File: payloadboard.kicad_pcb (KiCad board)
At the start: 2 copper layers, 46.8 x 46.8 mm, 15 parts, among them J1 TFM-110-12-L-D-A, J2 FLE-105-01-G-DV-A, J3 Micro_SD_Card, Q4 MMBT2907

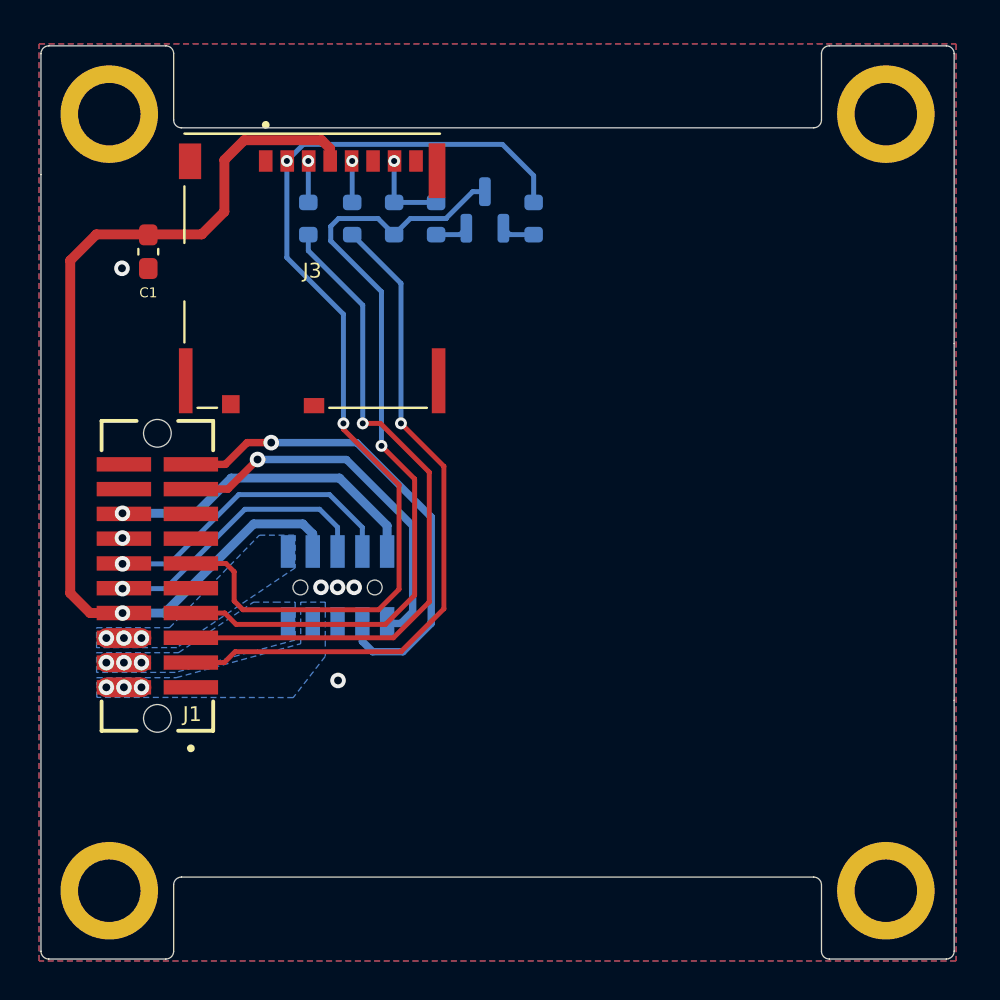
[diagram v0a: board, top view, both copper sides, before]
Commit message: Added 3.3V power regulator with enable pin and new stack connector
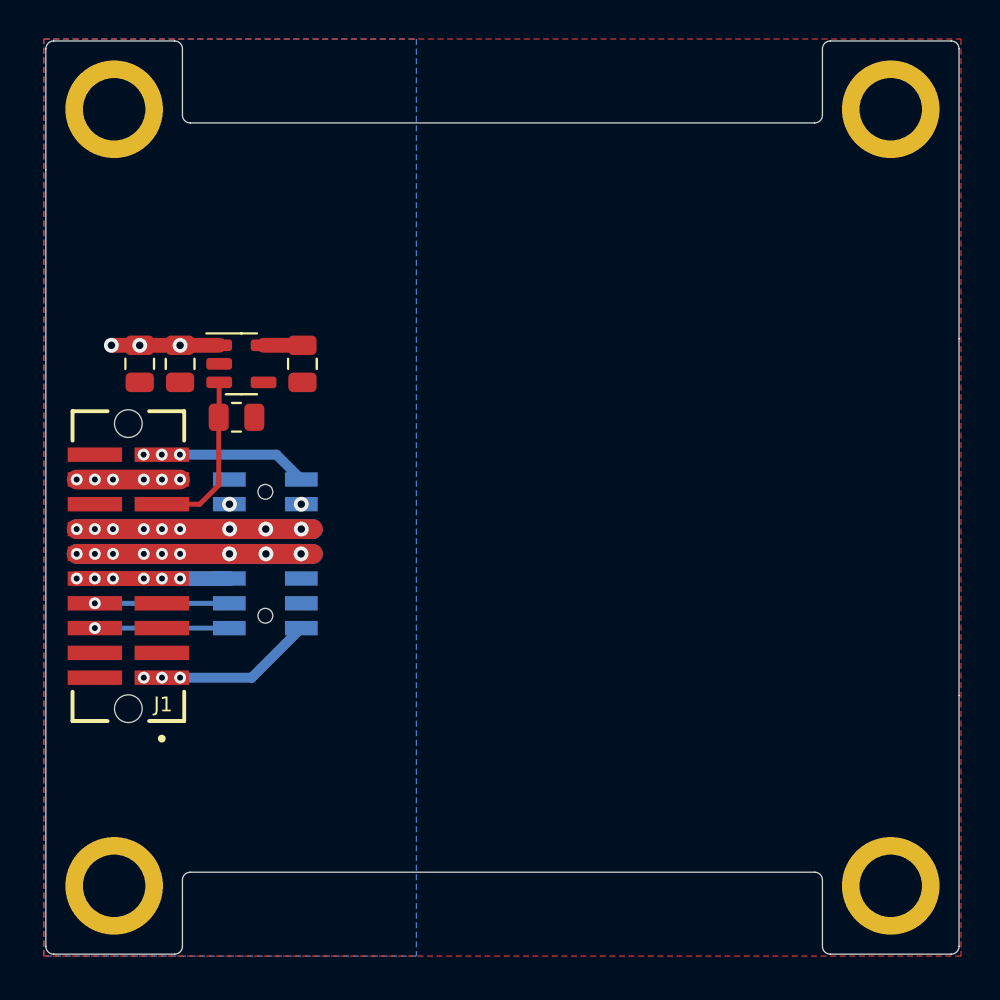
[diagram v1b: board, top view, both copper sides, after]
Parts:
- removed J3: Micro_SD_Card, cameraboard:MOLEX_503398-1892
- removed Q4: MMBT2907, Package_TO_SOT_SMD:SOT-23
- removed R11, R12: 1K, Resistor_SMD:R_0603_1608Metric
- removed R4, R7: 0, Resistor_SMD:R_0603_1608Metric
- removed R6: 4.7k, Resistor_SMD:R_0603_1608Metric
- added C2: 1uF, Capacitor_SMD:C_0805_2012Metric, F.Cu at (90.9, 56.8)
- added C3: 1uF, Capacitor_SMD:C_0805_2012Metric, F.Cu at (97.1, 56.8)
- added R1: 20K, Resistor_SMD:R_0805_2012Metric, F.Cu at (93.8, 59.6)
- added U1: AP2112K-3.3, Package_TO_SOT_SMD:SOT-23-5, F.Cu at (94.0, 56.8)
- C1: value 1uF -> 10uF; footprint Capacitor_SMD:C_0603_1608Metric_Pad1.08x0.95mm_HandSolder -> Capacitor_SMD:C_0805_2012Metric
- J2: value FLE-105-01-G-DV-A -> FLE-107-01-G-DV-A; footprint cameraboard:SAMTEC_FLE-105-01-G-DV-A -> cameraboard:SAMTEC_FLE-107-01-G-DV-A
- moved Ref** 6.76 mm to (107.9, 46.8)
- moved C1 5.76 mm to (88.8, 56.8), turned to -90 degrees
- moved J2 4.08 mm to (95.2, 66.6), turned to -90 degrees
- moved J1 1.57 mm to (88.2, 67.2)
- moved H1 0.35 mm to (87.5, 43.8)
- moved H2 0.35 mm to (127.3, 43.8)
- moved H3 0.35 mm to (127.3, 83.6)
- moved H4 0.35 mm to (87.5, 83.6)
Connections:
- C1 pad 1: GND -> /BATT_P
- C1 pad 2: +3V3 -> GND
- J1 pad 1: /HI_POW -> /COIL6_N
- J1 pad 10: /SCL3 -> +3V3
- J1 pad 11: SD_CS -> /BATT_N_SW
- J1 pad 12: /SDA3 -> /BATT_N_SW
- J1 pad 13: GND -> /BATT_P_SW
- J1 pad 14: GND -> /BATT_P_SW
- J1 pad 15: /CAM_EN -> /PAYLOAD_EN
- J1 pad 16: /VUSB -> GND
- J1 pad 17: /COIL6_N -> /BATT_P
- J1 pad 18: unconnected-(J1-Pad18) -> /BATT_P
- J1 pad 2: /BATT_P -> unconnected-(J1-Pad2)
- J1 pad 3: SCK -> GND
- J1 pad 4: /BATT_N_SW -> GND
- J1 pad 5: MOSI -> /UART_TX
- J1 pad 6: /BATT_P_SW -> /SCL1
- J1 pad 7: MISO -> /UART_RX
- J1 pad 8: +3V3 -> /SDA1
- J1 pad 9: /CAM_CS -> +3V3
- J2 pad 1: /BATT_N_SW -> unconnected-(J2-Pad1)
- J2 pad 10: /VUSB -> /BATT_P
- J2 pad 2: /BATT_P_SW -> /COIL6_P
- J2 pad 3: /BATT_P -> GND
- J2 pad 4: +3V3 -> GND
- J2 pad 5: GND -> /BATT_P_SW
- J2 pad 6: /SCL3 -> /BATT_P_SW
- J2 pad 7: /COIL6_P -> /BATT_N_SW
- J2 pad 8: /SDA3 -> /BATT_N_SW
- J2 pad 9: /COIL6_N -> +3V3
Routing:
- net SD_CS: track 52.3 -> 0.00 mm, vias 2 -> 0
- net MISO: track 42.4 -> 0.00 mm, vias 1 -> 0
- net +3V3: track 51.2 -> 13.1 mm, vias 1 -> 6
- net SCK: track 35.2 -> 0.00 mm, vias 1 -> 0
- net MOSI: track 34.9 -> 0.00 mm, vias 1 -> 0
- net /BATT_N_SW: track 1.80 -> 24.2 mm, vias 3 -> 9
- net /BATT_P_SW: track 1.80 -> 24.2 mm, vias 3 -> 9
- net /VUSB: track 16.6 -> 0.00 mm, vias 1 -> 0
- net /COIL6_P: track 25.1 -> 8.61 mm, vias 1 -> 3
- net /SDA3: track 15.7 -> 0.00 mm, vias 1 -> 0
- net /SCL3: track 14.3 -> 0.00 mm, vias 1 -> 0
- net /COIL6_N: track 19.4 -> 9.12 mm, vias 1 -> 3
- net /BATT_P: track 1.80 -> 10.8 mm, vias 3 -> 9
- net /PAYLOAD_EN: track 0.00 -> 8.44 mm
- net /SCL1: track 0.00 -> 6.90 mm, vias 0 -> 1
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- removed copper zone on B.Cu, net /BATT_N_SW
- removed copper zone on B.Cu, net /BATT_P_SW
- removed copper zone on B.Cu, net GND
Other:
- outline, holes or cut-outs redrawn
- board text added: "09-OCT-22"
- board text added: "Rev B2/01"
- board text removed: "08-SEP-22"
- board text removed: "Rev B1/02"

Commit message: Minor updates and export STEP / BOM
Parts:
- moved J2 0.40 mm to (95.1, 67.0)
- moved J1 0.14 mm to (88.1, 67.3)
- moved C2 0.14 mm to (90.8, 56.9)
- moved C3 0.14 mm to (97.0, 56.9)
- moved Ref** 0.14 mm to (107.8, 46.9)
- moved U1 0.14 mm to (93.9, 56.9)
- moved H1 0.14 mm to (87.4, 43.9)
- moved R1 0.14 mm to (93.7, 59.7)
- moved C1 0.14 mm to (88.7, 56.9)
- moved H4 0.14 mm to (87.4, 83.7)
- moved H2 0.14 mm to (127.2, 43.9)
- moved H3 0.14 mm to (127.2, 83.7)
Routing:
- net /COIL6_N: track 9.12 -> 8.07 mm, vias 3 -> 2
- net /BATT_P_SW: track 24.2 -> 25.2 mm
- net /BATT_N_SW: track 24.2 -> 25.2 mm
- net /COIL6_P: track 8.61 -> 7.80 mm, vias 3 -> 2
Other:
- outline, holes or cut-outs redrawn
- board text added: "06-NOV-22"
- board text removed: "09-OCT-22"
